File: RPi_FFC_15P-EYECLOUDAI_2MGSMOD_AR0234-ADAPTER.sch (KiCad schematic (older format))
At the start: 21 parts, among them J1 1-84952-5, J2 3-1734592-0, P1 53261-0371, P2 53261-0371, U1 MIC5259-1.8YD5-TR, U2 APX803-29SAG-7, X1 24MHz

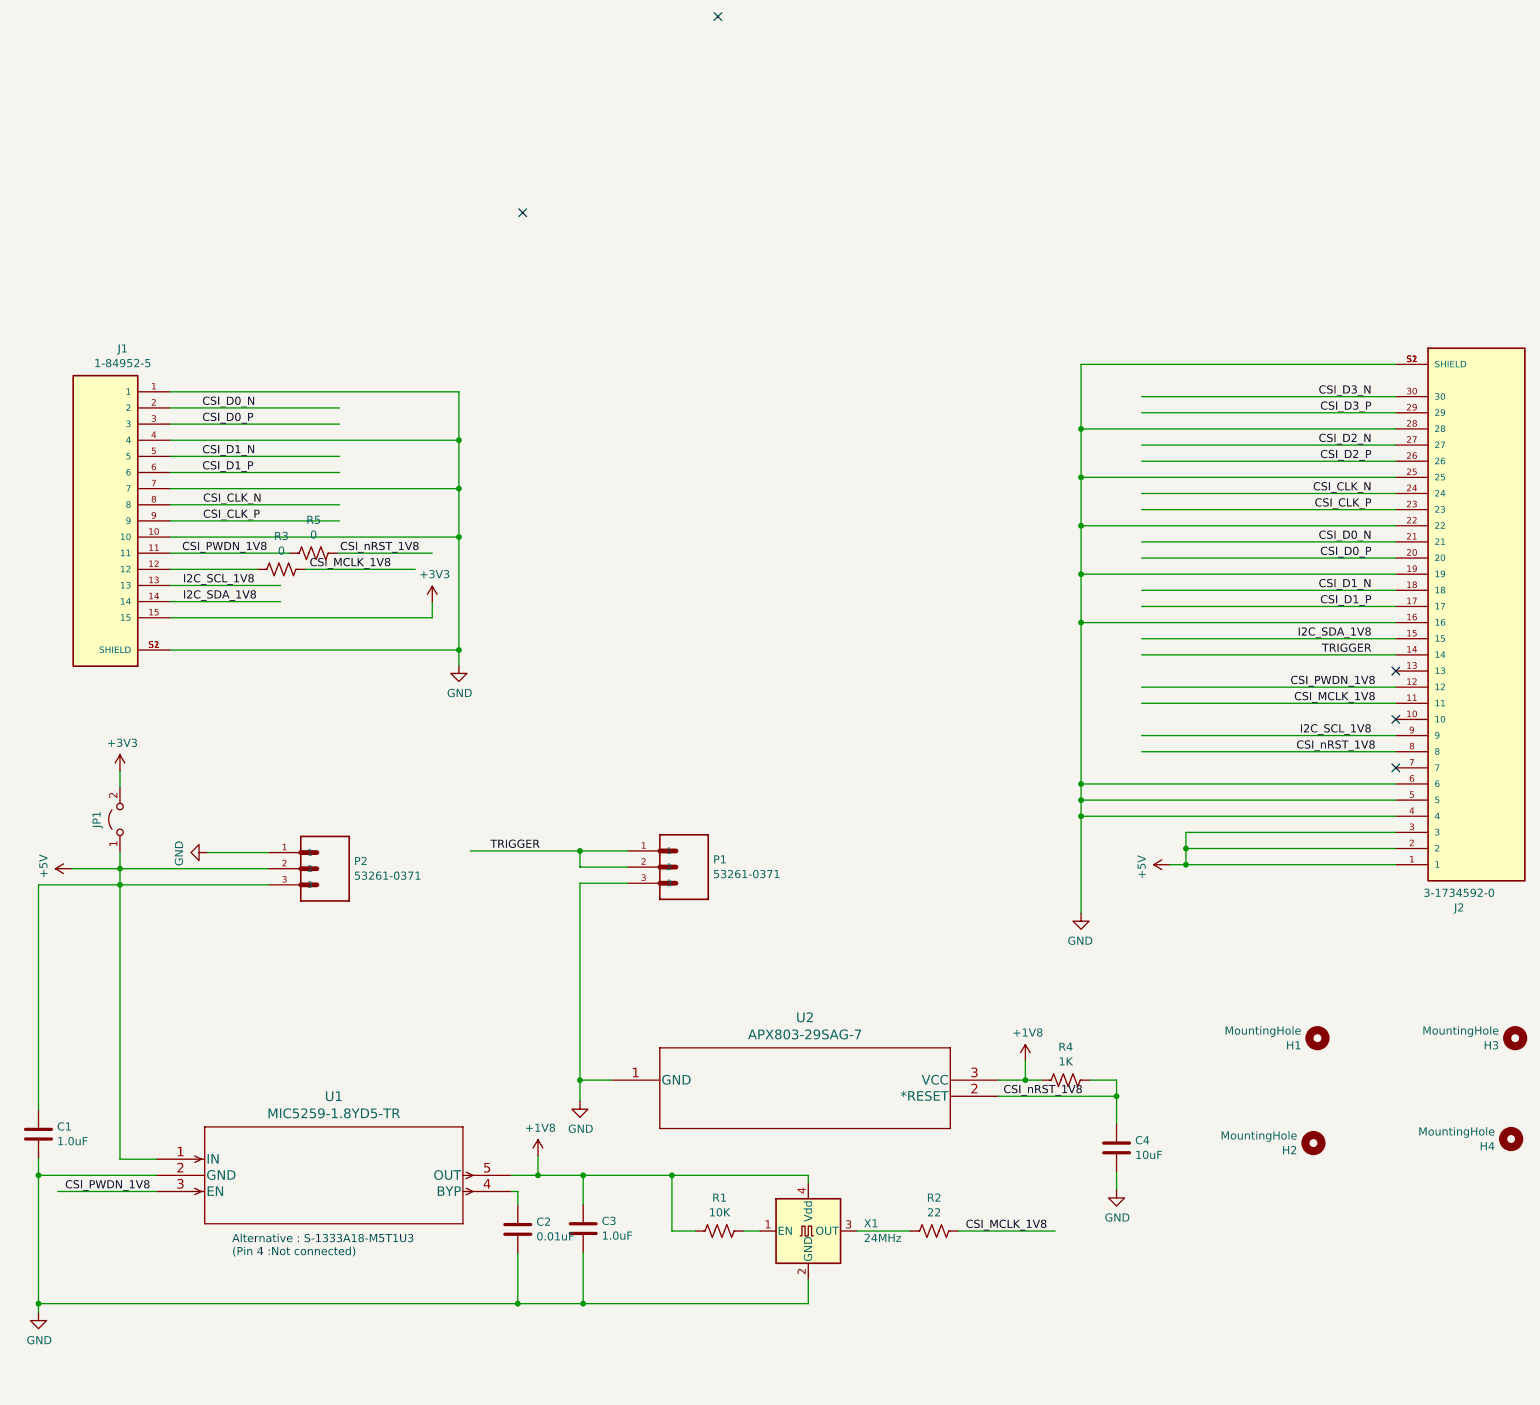
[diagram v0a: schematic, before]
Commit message: Add level shifters for 3V3<->1V8 signals
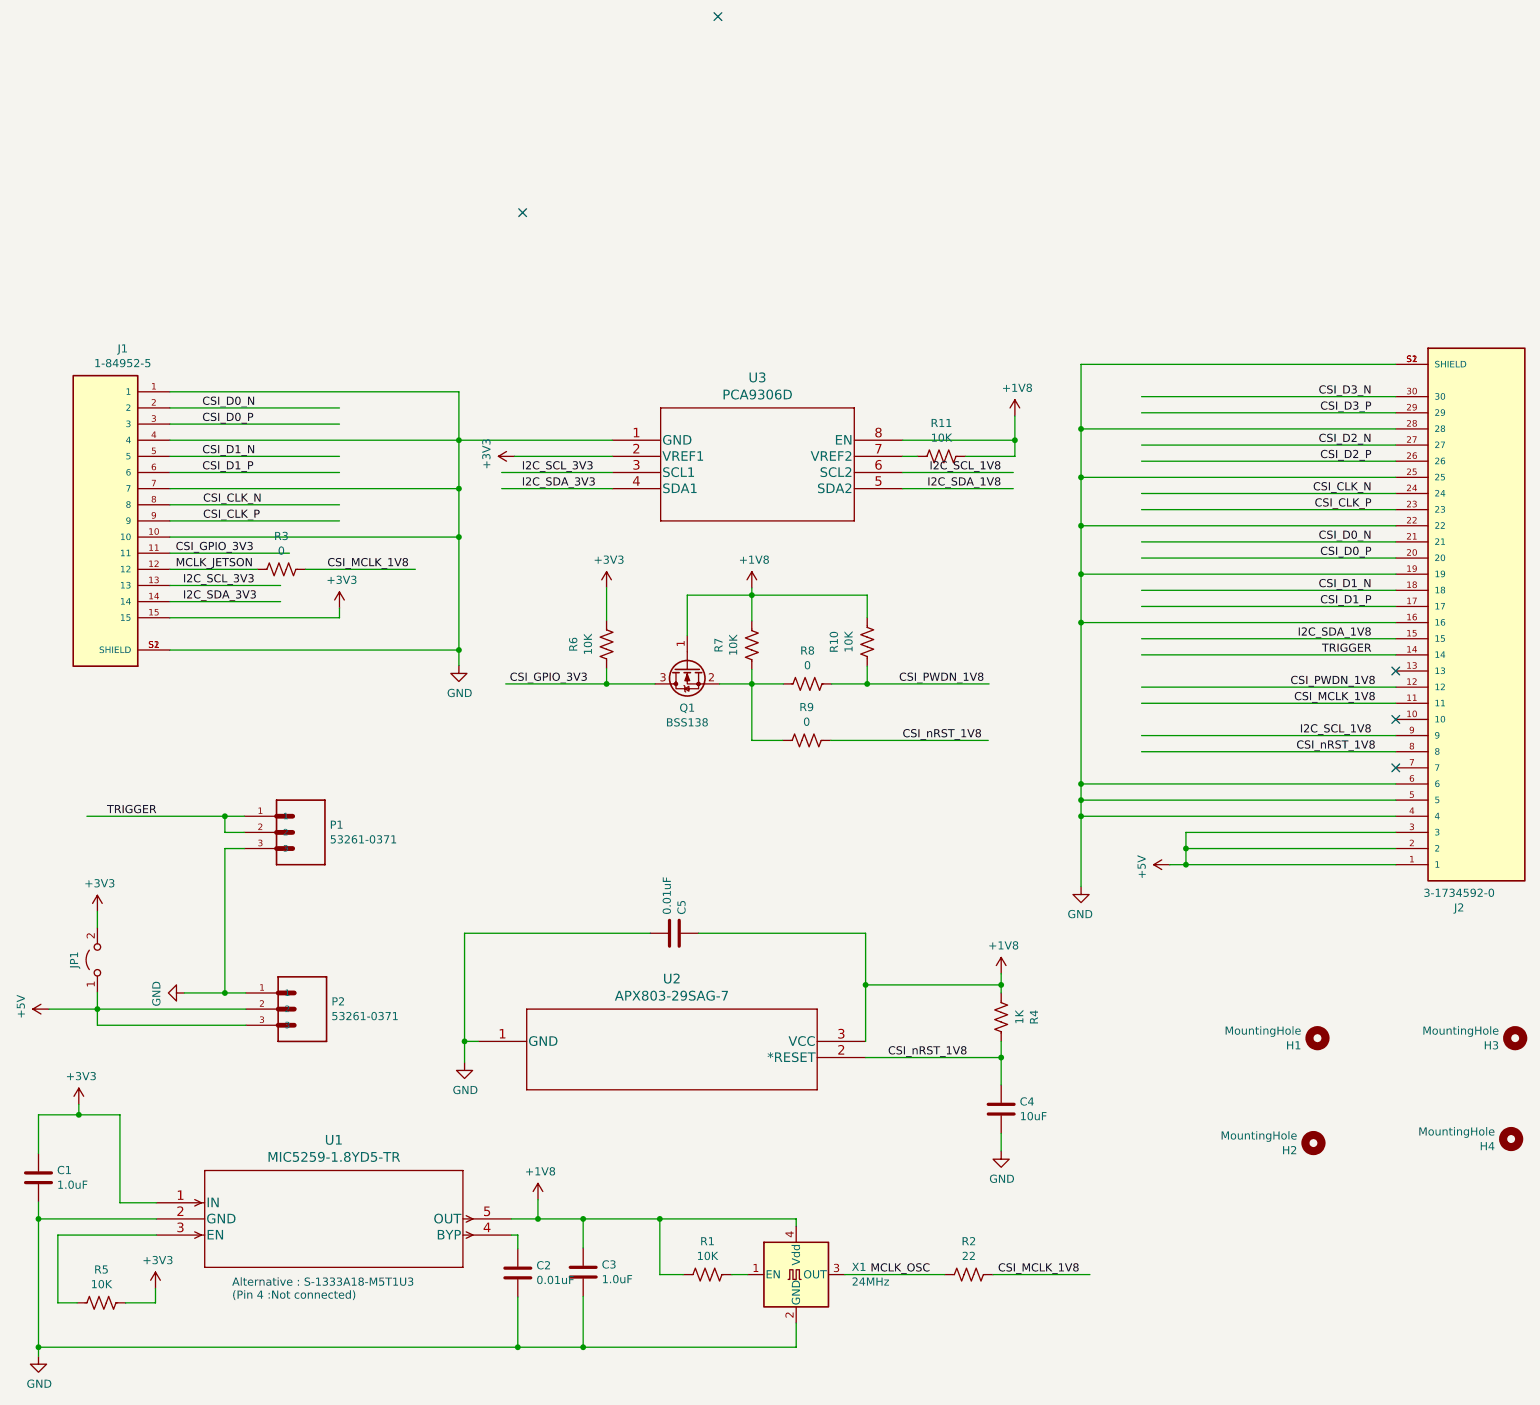
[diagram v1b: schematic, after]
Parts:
- added C5: 0.01uF, Capacitor_SMD:C_0603_1608Metric_Pad1.08x0.95mm_HandSolder, symbol Device:C
- added Q1: BSS138, Package_TO_SOT_SMD:SOT-23, symbol Transistor_FET:BSS138
- added R10, R11, R6, R7: 10K, Resistor_SMD:R_0603_1608Metric_Pad0.98x0.95mm_HandSolder, symbol Device:R_US
- added R8, R9: 0, Resistor_SMD:R_0603_1608Metric_Pad0.98x0.95mm_HandSolder, symbol Device:R_US
- added U3: PCA9306D, footprints:PCA9306D, symbol PCA9306D:PCA9306D_118
- R5: value 0 -> 10K
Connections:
- net labels added: CSI_GPIO_3V3, I2C_SCL_3V3, I2C_SDA_3V3, MCLK_JETSON, MCLK_OSC
- wire segments 116 -> 156
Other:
- moved on the sheet: C1, C2, C3, C4, JP1, P1, P2, R1, R2, R4, U1, U2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

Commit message: Add V1C
	Add 15pF capacitor at the ouput pin of the oscillator.
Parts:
- removed R2: 22, Resistor_SMD:R_0603_1608Metric_Pad0.98x0.95mm_HandSolder, symbol Device:R_US
- added C4: 15pF, Capacitor_SMD:C_0603_1608Metric_Pad1.08x0.95mm_HandSolder, symbol Device:C
- renumbered C4 to C6, R11 to R10, R10 to R2
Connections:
- net labels removed: MCLK_OSC
- wire segments 156 -> 159
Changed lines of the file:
@@
 Sheet 1 1
 Title "Adapter for EYECLOUDAI AR0234CS to RPi Cam Interface"
-Date "2021-11-12"
-Rev "V1B"
+Date "2024-08-11"
+Rev "V1C"
 Comp "TuxVision"
 Comment1 ""
@@
 Connection ~ 4375 6825
 $Comp
-L Device:C C4
+L Device:C C6
 U 1 1 65241586
 P 6965 5350
-F 0 "C4" H 7080 5396 50  0000 L CNN
+F 0 "C6" H 7080 5396 50  0000 L CNN
 F 1 "10uF" H 7080 5305 50  0000 L CNN
 F 2 "Capacitor_SMD:C_0603_1608Metric_Pad1.08x0.95mm_HandSolder" H 7003 5200 50  0001 C CNN
@@
 Wire Wire Line
 	6965 5500 6965 5610
-$Comp
-L Device:R_US R3
-U 1 1 6525784F
-P 2505 2005
-F 0 "R3" V 2300 2005 50  0000 C CNN
-F 1 "0" V 2391 2005 50  0000 C CNN
-F 2 "Resistor_SMD:R_0603_1608Metric_Pad0.98x0.95mm_HandSolder" V 2545 1995 50  0001 C CNN
-F 3 "~" H 2505 2005 50  0001 C CNN
-	1    2505 2005
-	0    1    1    0
-$EndComp
 $Comp
 L Device:R_US R1
@@
 	0    1    1    0
 $EndComp
-$Comp
-L Device:R_US R2
-U 1 1 652653E6
-P 6765 6375
-F 0 "R2" V 6560 6375 50  0000 C CNN
-F 1 "22" V 6651 6375 50  0000 C CNN
-F 2 "Resistor_SMD:R_0603_1608Metric_Pad0.98x0.95mm_HandSolder" V 6805 6365 50  0001 C CNN
-F 3 "~" H 6765 6375 50  0001 C CNN
-	1    6765 6375
-	0    1    1    0
-$EndComp
 Wire Wire Line
 	5395 6375 5295 6375
@@
 Text Label 7450 6375 2    50   ~ 0
 CSI_MCLK_1V8
-Wire Wire Line
-	6915 6375 7515 6375
 Wire Wire Line
 	1815 2105 2500 2105
@@
 	7050 1205 7050 1055
 $Comp
-L Device:R_US R11
+L Device:R_US R10
 U 1 1 6537FE10
 P 6595 1305
-F 0 "R11" V 6390 1305 50  0000 C CNN
+F 0 "R10" V 6390 1305 50  0000 C CNN
 F 1 "10K" V 6481 1305 50  0000 C CNN
 F 2 "Resistor_SMD:R_0603_1608Metric_Pad0.98x0.95mm_HandSolder" V 6635 1295 50  0001 C CNN
@@
 Text Label 1850 2005 0    50   ~ 0
 MCLK_JETSON
-Text Label 6155 6375 0    50   ~ 0
-MCLK_OSC
 Wire Wire Line
 	4095 6030 4375 6030
@@
 Wire Wire Line
 	5695 6825 4375 6825
-Wire Wire Line
-	5995 6375 6615 6375
 $Comp
 L Device:R_US R5
@@
 CSI_nRST_1V8
 $Comp
-L Device:R_US R10
+L Device:R_US R2
 U 1 1 655895EC
 P 6135 2455
-F 0 "R10" V 5930 2455 50  0000 C CNN
+F 0 "R2" V 5930 2455 50  0000 C CNN
 F 1 "10K" V 6021 2455 50  0000 C CNN
 F 2 "Resistor_SMD:R_0603_1608Metric_Pad0.98x0.95mm_HandSolder" V 6175 2445 50  0001 C CNN
@@
 Wire Wire Line
 	6135 2715 6890 2715
+$Comp
+L Device:C C4
+U 1 1 66B9F662
+P 6400 6585
+F 0 "C4" H 6515 6631 50  0000 L CNN
+F 1 "15pF" H 6515 6540 50  0000 L CNN
+F 2 "Capacitor_SMD:C_0603_1608Metric_Pad1.08x0.95mm_HandSolder" H 6438 6435 50  0001 C CNN
+F 3 "~" H 6400 6585 50  0001 C CNN
+	1    6400 6585
+	1    0    0    -1
+$EndComp
+Wire Wire Line
+	6400 6435 6400 6375
+Wire Wire Line
+	5995 6375 6400 6375
+Connection ~ 6400 6375
+Wire Wire Line
+	6400 6375 7515 6375
+Wire Wire Line
+	5695 6825 6400 6825
+Wire Wire Line
+	6400 6825 6400 6735
+Connection ~ 5695 6825
+$Comp
+L Device:R_US R3
+U 1 1 6525784F
+P 2505 2005
+F 0 "R3" V 2300 2005 50  0000 C CNN
+F 1 "0" V 2391 2005 50  0000 C CNN
+F 2 "Resistor_SMD:R_0603_1608Metric_Pad0.98x0.95mm_HandSolder" V 2545 1995 50  0001 C CNN
+F 3 "~" H 2505 2005 50  0001 C CNN
+	1    2505 2005
+	0    1    1    0
+$EndComp
 $EndSCHEMATC
